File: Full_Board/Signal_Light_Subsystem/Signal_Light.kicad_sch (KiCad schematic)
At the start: 3 parts, among them J24 OQ0212500000G, U19 RUC002N05T116

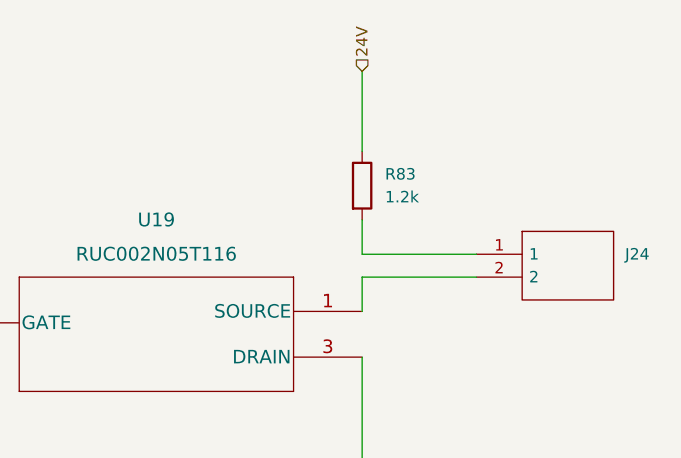
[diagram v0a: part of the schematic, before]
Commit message: Replace small resistors/capacitors with through-hole; fix DRC aside from electromagnet and MUXes
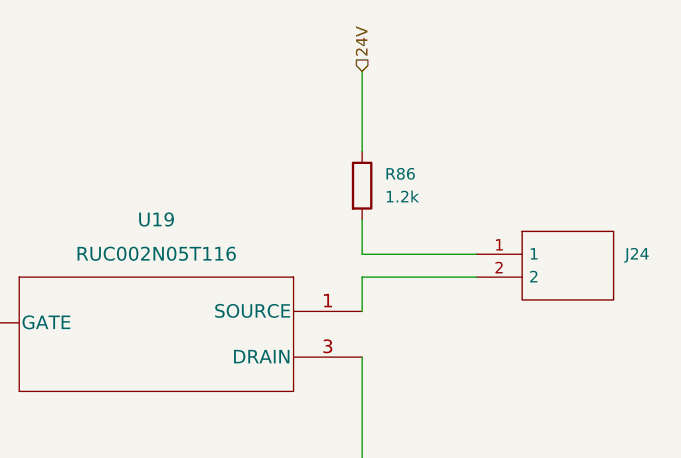
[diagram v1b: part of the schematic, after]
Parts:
- renumbered R83 to R86
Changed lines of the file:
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@@
   (symbol (lib_id "Device:R") (at 162.56 82.55 0) (unit 1)
     (in_bom yes) (on_board yes) (fields_autoplaced)
-    (property "Reference" "R83" (id 0) (at 165.1 81.2799 0)
+    (property "Reference" "R86" (id 0) (at 165.1 81.2799 0)
       (effects (font (size 1.27 1.27)) (justify left))
     )

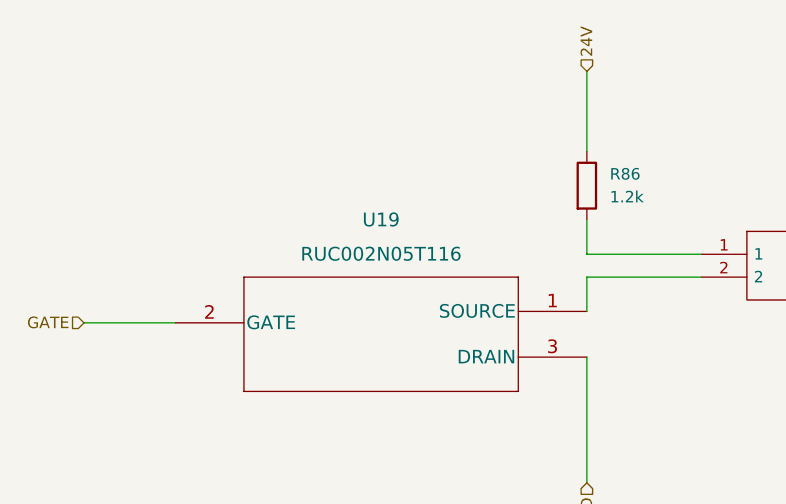
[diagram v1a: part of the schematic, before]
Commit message: Replace MUX/DEMUX; DRC passes aside from electromagnet
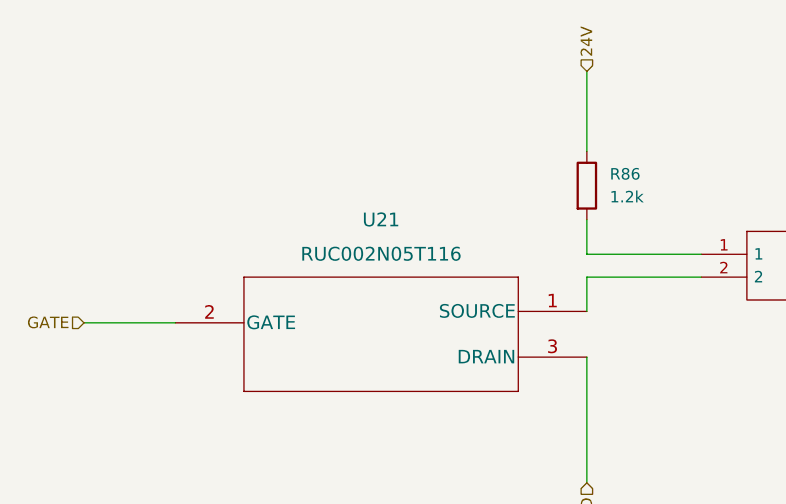
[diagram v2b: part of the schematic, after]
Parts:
- renumbered U19 to U21
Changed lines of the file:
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@@
   (symbol (lib_id "RUC002N05T116:RUC002N05T116") (at 116.84 97.79 0) (unit 1)
     (in_bom yes) (on_board yes) (fields_autoplaced)
-    (property "Reference" "U19" (id 0) (at 139.7 86.36 0)
+    (property "Reference" "U21" (id 0) (at 139.7 86.36 0)
       (effects (font (size 1.524 1.524)))
     )

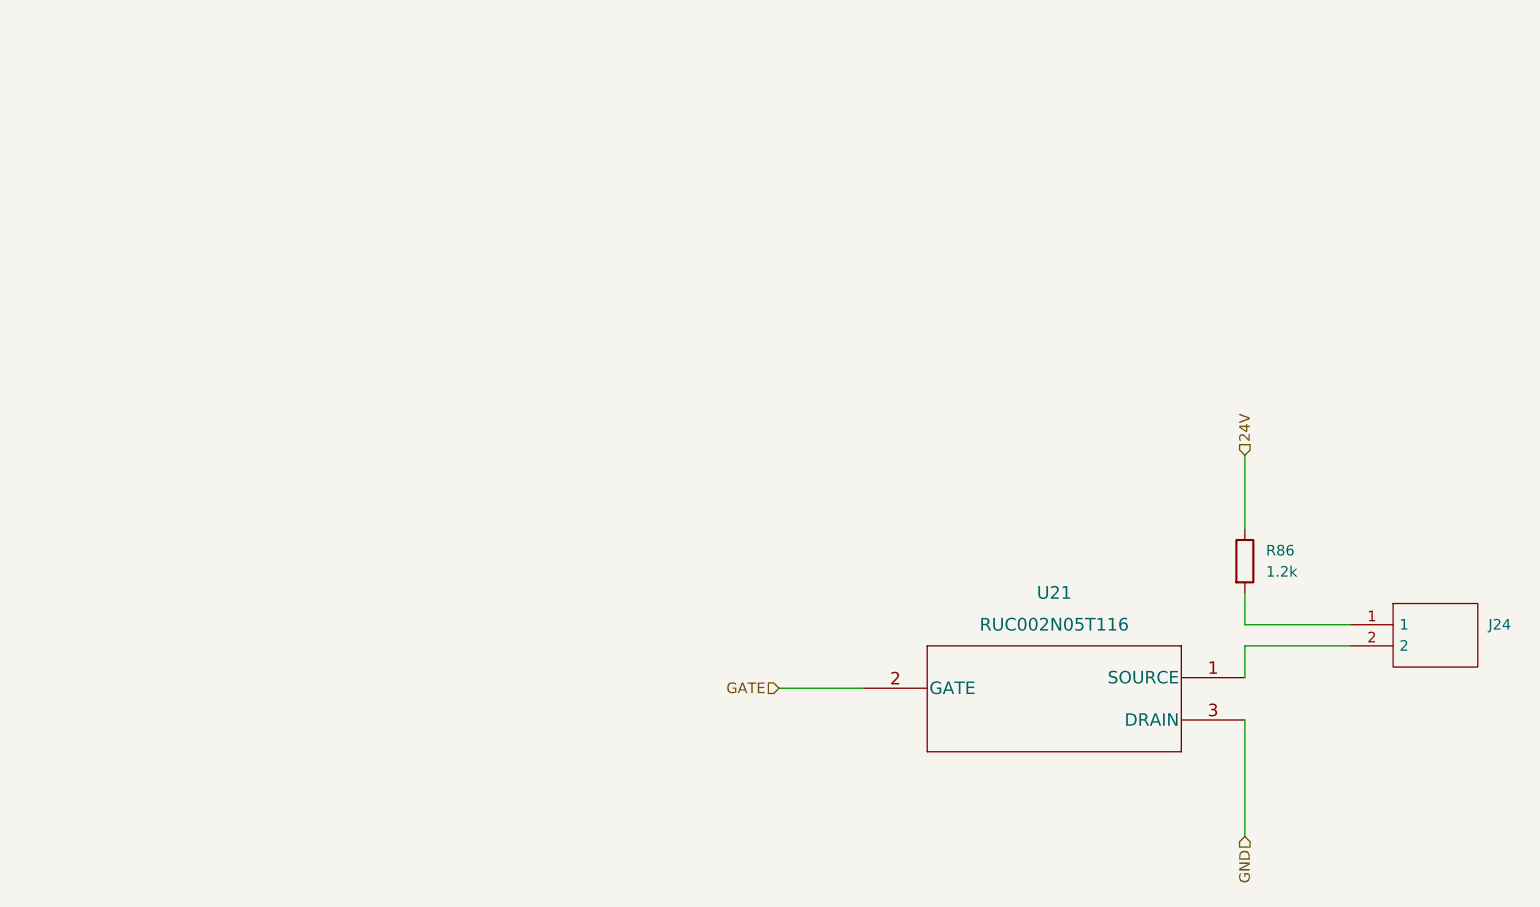
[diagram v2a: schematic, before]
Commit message: Cleanup all schematics and project libs
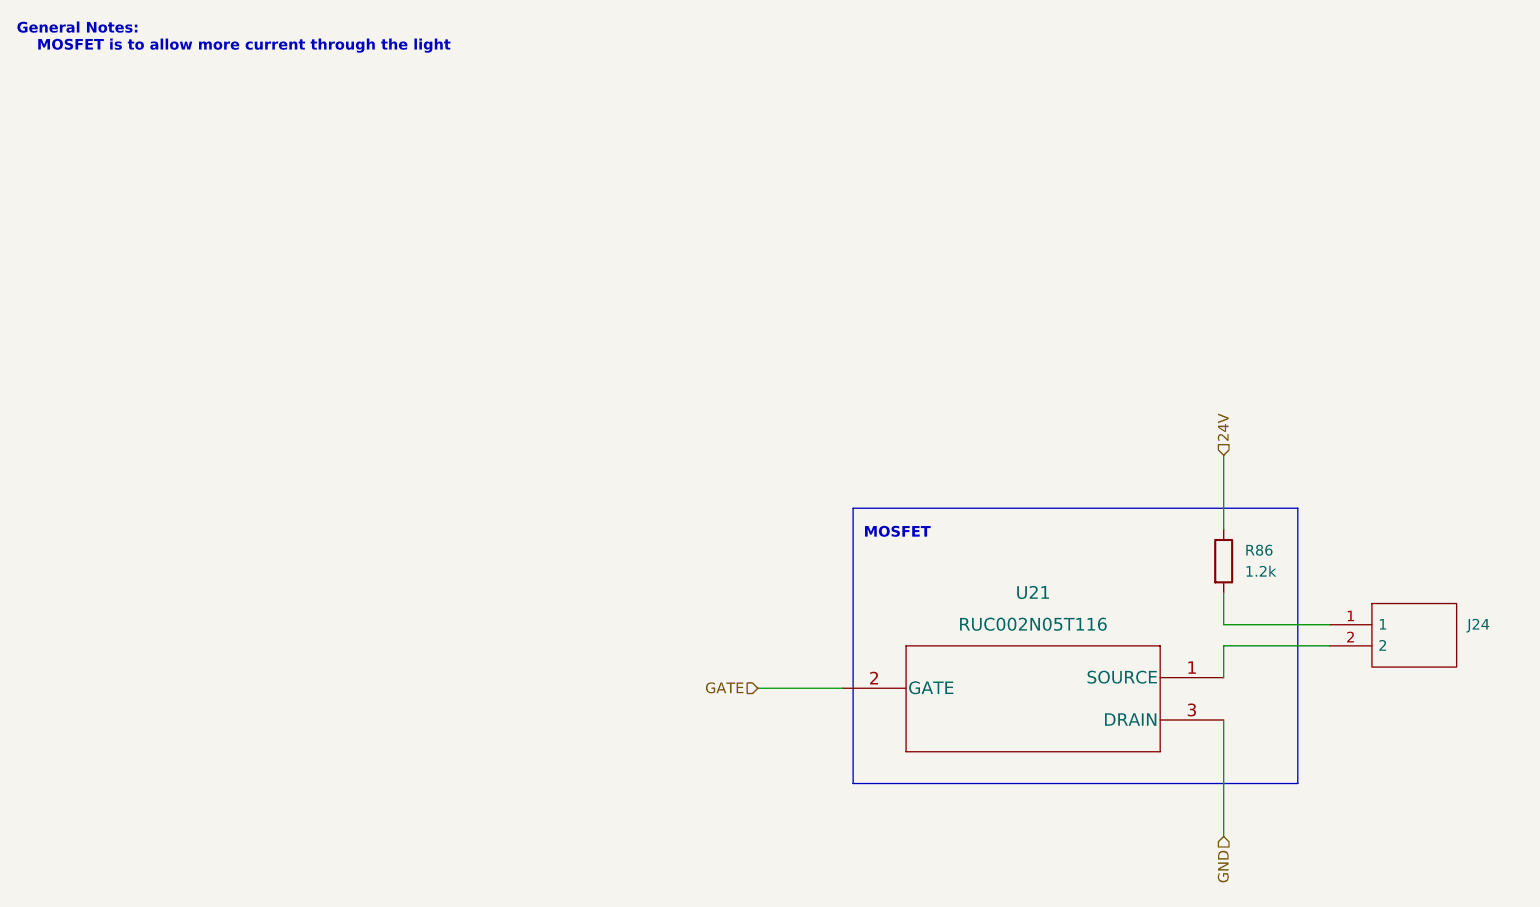
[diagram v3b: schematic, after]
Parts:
- J24: Height 9.2 -> (none); Manufacturer's Part Number (none) -> OQ0212500000G; Manufacturer_Name Amphenol -> (none); Manufacturer_Part_Number OQ0212500000G -> (none); Mouser Link (none) -> https://www.mouser.com/ProductDetail/Amphenol-Anytek/OQ0212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; Mouser Price/Stock https://www.mouser.co.uk/ProductDetail/Amphenol-Anytek/OQ02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 -> (none)
- R86: Digikey Link (none) -> FUN Kit; Digikey Part Number (none) -> FUN Kit; Manufacturer's Part Number (none) -> FUN Kit; Mouser Link (none) -> FUN Kit
- U21: footprint RUC002N05116:RUC002N05T116 -> SOT23-3_ROM; Manufacturer's Part Number (none) -> RUC002N05T116; Manufacturers Part Number RUC002N05T116 -> (none); Mouser Link (none) -> https://www.mouser.com/ProductDetail/ROHM-Semiconductor/RUC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; Mouser Part Number (none) -> 755-RUC002N05T116
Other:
- note added: "General Notes: MOSFET is to allow more current through the light"
- note added: "MOSFET"
- moved on the sheet: J24, R86, U21
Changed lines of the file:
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@@
 (kicad_sch (version 20211123) (generator eeschema)
   (paper "A4")
-  (wire (pts (xy 162.56 90.17) (xy 162.56 86.36))
+  (wire (pts (xy 160.02 90.17) (xy 160.02 86.36))
     (stroke (width 0) (type default) (color 0 0 0 0))
   )
-  (wire (pts (xy 106.68 97.79) (xy 116.84 97.79))
+  (polyline (pts (xy 115.57 109.22) (xy 168.91 109.22))
     (stroke (width 0) (type default) (color 0 0 0 0))
   )
-  (wire (pts (xy 175.26 92.71) (xy 162.56 92.71))
+  (wire (pts (xy 104.14 97.79) (xy 114.3 97.79))
     (stroke (width 0) (type default) (color 0 0 0 0))
   )
-  (wire (pts (xy 162.56 69.85) (xy 162.56 78.74))
+  (wire (pts (xy 172.72 92.71) (xy 160.02 92.71))
     (stroke (width 0) (type default) (color 0 0 0 0))
   )
-  (wire (pts (xy 162.56 92.71) (xy 162.56 96.52))
+  (wire (pts (xy 160.02 69.85) (xy 160.02 78.74))
     (stroke (width 0) (type default) (color 0 0 0 0))
   )
-  (wire (pts (xy 162.56 101.6) (xy 162.56 115.57))
+  (wire (pts (xy 160.02 92.71) (xy 160.02 96.52))
     (stroke (width 0) (type default) (color 0 0 0 0))
   )
-  (wire (pts (xy 175.26 90.17) (xy 162.56 90.17))
+  (polyline (pts (xy 115.57 76.2) (xy 115.57 109.22))
     (stroke (width 0) (type default) (color 0 0 0 0))
   )
-  (hierarchical_label "GATE" (shape input) (at 106.68 97.79 180)
+  (wire (pts (xy 160.02 101.6) (xy 160.02 115.57))
+    (stroke (width 0) (type default) (color 0 0 0 0))
+  )
+  (polyline (pts (xy 168.91 109.22) (xy 168.91 76.2))
+    (stroke (width 0) (type default) (color 0 0 0 0))
+  )
+  (polyline (pts (xy 115.57 76.2) (xy 168.91 76.2))
+    (stroke (width 0) (type default) (color 0 0 0 0))
+  )
+  (wire (pts (xy 172.72 90.17) (xy 160.02 90.17))
+    (stroke (width 0) (type default) (color 0 0 0 0))
+  )
+  (text "MOSFET" (at 116.84 80.01 0)
+    (effects (font (size 1.27 1.27) bold) (justify left bottom))
+  )
+  (text "General Notes:\n	MOSFET is to allow more current through the light"
+    (at 15.24 21.59 0)
+    (effects (font (size 1.27 1.27) bold) (justify left bottom))
+  )
+  (hierarchical_label "GATE" (shape input) (at 104.14 97.79 180)
     (effects (font (size 1.27 1.27)) (justify right))
   )
-  (hierarchical_label "GND" (shape input) (at 162.56 115.57 270)
+  (hierarchical_label "GND" (shape input) (at 160.02 115.57 270)
     (effects (font (size 1.27 1.27)) (justify right))
   )
-  (hierarchical_label "24V" (shape input) (at 162.56 69.85 90)
+  (hierarchical_label "24V" (shape input) (at 160.02 69.85 90)
     (effects (font (size 1.27 1.27)) (justify left))
   )
-  (symbol (lib_id "OQ0212500000G:OQ0212500000G") (at 175.26 90.17 0) (unit 1)
+  (symbol (lib_id "OQ0212500000G:OQ0212500000G") (at 172.72 90.17 0) (unit 1)
     (in_bom yes) (on_board yes) (fields_autoplaced)
-    (property "Reference" "J24" (id 0) (at 191.77 90.1699 0)
+    (property "Reference" "J24" (id 0) (at 189.23 90.1699 0)
       (effects (font (size 1.27 1.27)) (justify left))
     )
-    (property "Value" "OQ0212500000G" (id 1) (at 191.77 92.7099 0)
+    (property "Value" "OQ0212500000G" (id 1) (at 189.23 92.7099 0)
       (effects (font (size 1.27 1.27)) (justify left) hide)
     )
-    (property "Footprint" "OQ0212500000G:OQ0212500000G" (id 2) (at 191.77 87.63 0)
+    (property "Footprint" "OQ0212500000G:OQ0212500000G" (id 2) (at 189.23 87.63 0)
       (effects (font (size 1.27 1.27)) (justify left) hide)
     )
-    (property "Datasheet" "https://datasheet.datasheetarchive.com/originals/distributors/DKDS-9/178262.pdf" (id 3) (at 191.77 90.17 0)
+    (property "Datasheet" "https://datasheet.datasheetarchive.com/originals/distributors/DKDS-9/178262.pdf" (id 3) (at 189.23 90.17 0)
       (effects (font (size 1.27 1.27)) (justify left) hide)
     )
-    (property "Manufacturer_Part_Number" "OQ0212500000G" (id 4) (at 191.77 105.41 0)
+    (property "Digikey Part Number" "609-4981-ND" (id 5) (at 172.72 90.17 0)
+      (effects (font (size 1.27 1.27)) hide)
+    )
+    (property "Mouser Part Number" "649-220107-C021A01LF" (id 6) (at 189.23 97.79 0)
       (effects (font (size 1.27 1.27)) (justify left) hide)
     )
-    (property "Digikey Part Number" "609-4981-ND" (id 5) (at 175.26 90.17 0)
+    (property "Digikey Link" "https://www.digikey.com/en/products/detail/amphenol-anytek/OQ0212500000G/4242016" (id 7) (at 172.72 90.17 0)
       (effects (font (size 1.27 1.27)) hide)
     )
-    (property "Mouser Part Number" "649-220107-C021A01LF" (id 6) (at 191.77 97.79 0)
-      (effects (font (size 1.27 1.27)) (justify left) hide)
-    )
-    (property "Digikey Link" "https://www.digikey.com/en/products/detail/amphenol-anytek/OQ0212500000G/4242016" (id 7) (at 175.26 90.17 0)
+    (property "Mouser Link" "https://www.mouser.com/ProductDetail/Amphenol-Anytek/OQ0212500000G?qs=Mv7BduZupUhn3/Ke8nJdbQ%3D%3D" (id 8) (at 172.72 90.17 0)
       (effects (font (size 1.27 1.27)) hide)
     )
-    (property "Mouser Link" "" (id 8) (at 175.26 90.17 0)
-      (effects (font (size 1.27 1.27)) hide)
-    )
-    (property "Description" "Pluggable Terminal Blocks 2P 3.50MM HDR STR PLUGGABLE TERM BLK" (id 9) (at 191.77 92.71 0)
-      (effects (font (size 1.27 1.27)) (justify left) hide)
-    )
-    (property "Height" "9.2" (id 10) (at 191.77 95.25 0)
-      (effects (font (size 1.27 1.27)) (justify left) hide)
-    )
-    (property "Mouser Price/Stock" "https://www.mouser.co.uk/ProductDetail/Amphenol-Anytek/OQ0212500000G?qs=Mv7BduZupUhn3%2FKe8nJdbQ%3D%3D" (id 11) (at 191.77 100.33 0)
-      (effects (font (size 1.27 1.27)) (justify left) hide)
-    )
-    (property "Manufacturer_Name" "Amphenol" (id 12) (at 191.77 102.87 0)
+    (property "Manufacturer's Part Number" "OQ0212500000G" (id 9) (at 189.23 105.41 0)
       (effects (font (size 1.27 1.27)) (justify left) hide)
     )
@@
     (pin "2")
   )
-  (symbol (lib_id "RUC002N05T116:RUC002N05T116") (at 116.84 97.79 0) (unit 1)
+  (symbol (lib_id "RUC002N05T116:RUC002N05T116") (at 114.3 97.79 0) (unit 1)
     (in_bom yes) (on_board yes) (fields_autoplaced)
-    (property "Reference" "U21" (id 0) (at 139.7 86.36 0)
+    (property "Reference" "U21" (id 0) (at 137.16 86.36 0)
       (effects (font (size 1.524 1.524)))
     )
-    (property "Value" "RUC002N05T116" (id 1) (at 139.7 90.17 0)
+    (property "Value" "RUC002N05T116" (id 1) (at 137.16 90.17 0)
       (effects (font (size 1.524 1.524)))
     )
-    (property "Footprint" "RUC002N05116:RUC002N05T116" (id 2) (at 139.7 91.694 0)
+    (property "Footprint" "SOT23-3_ROM" (id 2) (at 137.16 91.694 0)
       (effects (font (size 1.524 1.524)) hide)
     )
-    (property "Datasheet" "https://fscdn.rohm.com/en/products/databook/datasheet/discrete/transistor/mosfet/ruc002n05t116-e.pdf" (id 3) (at 116.84 97.79 0)
+    (property "Datasheet" "https://fscdn.rohm.com/en/products/databook/datasheet/discrete/transistor/mosfet/ruc002n05t116-e.pdf" (id 3) (at 114.3 97.79 0)
       (effects (font (size 1.524 1.524)) hide)
     )
-    (property "Manufacturers Part Number" "RUC002N05T116" (id 4) (at 116.84 97.79 0)
+    (property "Digikey Part Number" "RUC002N05T116DKR-ND" (id 5) (at 114.3 97.79 0)
       (effects (font (size 1.27 1.27)) hide)
     )
-    (property "Digikey Part Number" "RUC002N05T116DKR-ND" (id 5) (at 116.84 97.79 0)
+    (property "Mouser Part Number" "755-RUC002N05T116" (id 6) (at 114.3 97.79 0)
       (effects (font (size 1.27 1.27)) hide)
     )
-    (property "Mouser Part Number" "" (id 6) (at 116.84 97.79 0)
+    (property "Digikey Link" "https://www.digikey.com/en/products/detail/rohm-semiconductor/RUC002N05T116/4004578" (id 7) (at 114.3 97.79 0)
       (effects (font (size 1.27 1.27)) hide)
     )
-    (property "Digikey Link" "https://www.digikey.com/en/products/detail/rohm-semiconductor/RUC002N05T116/4004578" (id 7) (at 116.84 97.79 0)
+    (property "Mouser Link" "https://www.mouser.com/ProductDetail/ROHM-Semiconductor/RUC002N05T116?qs=QcFhgjUTvvohwn8zGzFgTQ%3D%3D" (id 8) (at 114.3 97.79 0)
       (effects (font (size 1.27 1.27)) hide)
     )
-    (property "Mouser Link" "" (id 8) (at 116.84 97.79 0)
+    (property "Manufacturer's Part Number" "RUC002N05T116" (id 9) (at 114.3 97.79 0)
       (effects (font (size 1.27 1.27)) hide)
     )
@@
     (pin "3")
   )
-  (symbol (lib_id "Device:R") (at 162.56 82.55 0) (unit 1)
+  (symbol (lib_id "Device:R") (at 160.02 82.55 0) (unit 1)
     (in_bom yes) (on_board yes) (fields_autoplaced)
-    (property "Reference" "R86" (id 0) (at 165.1 81.2799 0)
+    (property "Reference" "R86" (id 0) (at 162.56 81.2799 0)
       (effects (font (size 1.27 1.27)) (justify left))
     )
-    (property "Value" "1.2k" (id 1) (at 165.1 83.8199 0)
+    (property "Value" "1.2k" (id 1) (at 162.56 83.8199 0)
       (effects (font (size 1.27 1.27)) (justify left))
     )
-    (property "Footprint" "Resistor_THT:R_Axial_DIN0207_L6.3mm_D2.5mm_P10.16mm_Horizontal" (id 2) (at 160.782 82.55 90)
+    (property "Footprint" "Resistor_THT:R_Axial_DIN0207_L6.3mm_D2.5mm_P10.16mm_Horizontal" (id 2) (at 158.242 82.55 90)
       (effects (font (size 1.27 1.27)) hide)
     )
-    (property "Datasheet" "~" (id 3) (at 162.56 82.55 0)
+    (property "Datasheet" "~" (id 3) (at 160.02 82.55 0)
       (effects (font (size 1.27 1.27)) hide)
     )
+    (property "Digikey Link" "FUN Kit" (id 4) (at 160.02 82.55 0)
+      (effects (font (size 1.27 1.27)) hide)
+    )
+    (property "Digikey Part Number" "FUN Kit" (id 5) (at 160.02 82.55 0)
+      (effects (font (size 1.27 1.27)) hide)
+    )
+    (property "Manufacturer's Part Number" "FUN Kit" (id 6) (at 160.02 82.55 0)
+      (effects (font (size 1.27 1.27)) hide)
+    )
+    (property "Mouser Link" "FUN Kit" (id 7) (at 160.02 82.55 0)
+      (effects (font (size 1.27 1.27)) hide)
+    )
